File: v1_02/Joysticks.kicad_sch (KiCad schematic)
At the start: 29 parts, among them J10 DB9_Male_MountingHoles, J11 DA15_Socket_MountingHoles, J13 Aliexpress ADS1115 module, J15 Conn_01x01_Pin, J17 Conn_01x03_Pin, U4 74LV165A, U5 74LV165A, U6 LM4040D20ILPR, U7 PCF8583T, Y1 32.768 kHz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

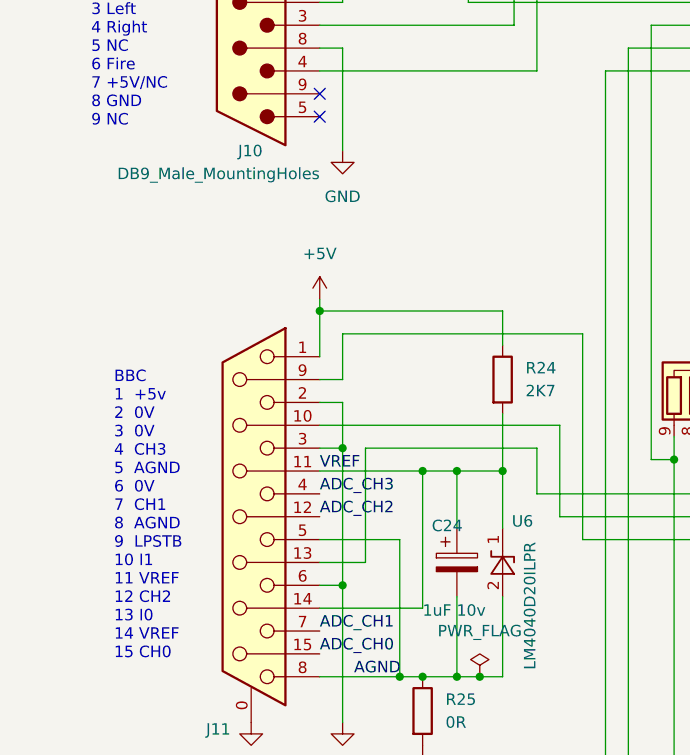
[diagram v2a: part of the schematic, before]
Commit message: v1_02: Increase PS/2 + Tang hole sizes; corrected U6 symbol
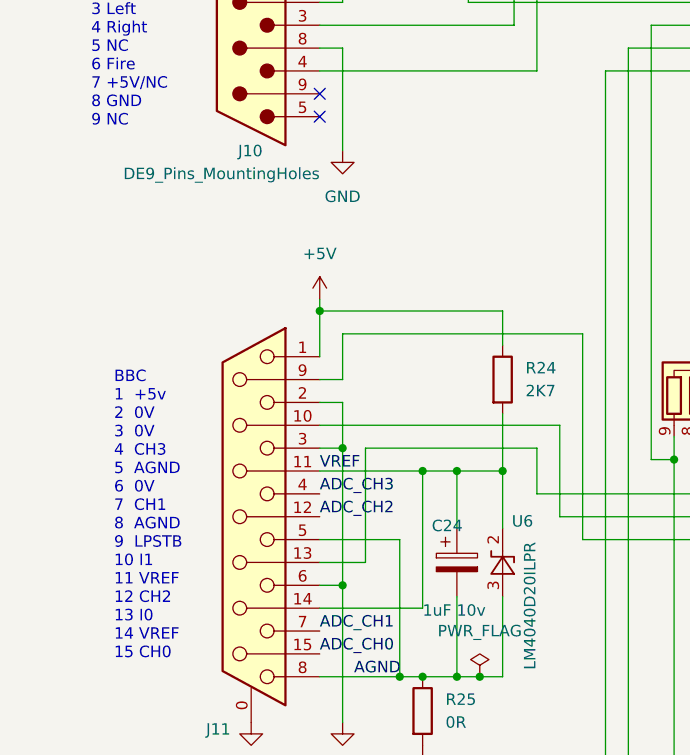
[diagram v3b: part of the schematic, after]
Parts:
- J10: value DB9_Male_MountingHoles -> DE9_Pins_MountingHoles
- U6: footprint Package_TO_SOT_THT:TO-92L_HandSolder -> Package_TO_SOT_THT:TO-92_HandSolder; symbol Reference_Voltage:LM4040DBZ-2.0 -> Reference_Voltage:LM4040LP-2.0
- Y1: footprint Crystal:Crystal_SMD_3215-2Pin_3.2x1.5mm -> TangNano20k:Crystal_SMD_3215-2Pin_3.2x1.5mm
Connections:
- net AGND: now also U6.3 (A); no longer U6.2 (A)
- net VREF: now also U6.2 (K); no longer U6.1 (K)
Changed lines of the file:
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@@
 			)
 		)
-		(property "Footprint" "Crystal:Crystal_SMD_3215-2Pin_3.2x1.5mm"
+		(property "Footprint" "TangNano20k:Crystal_SMD_3215-2Pin_3.2x1.5mm"
 			(at 248.92 106.68 0)
 			(effects
@@
 	)
 	(symbol
-		(lib_id "Reference_Voltage:LM4040DBZ-2.0")
+		(lib_id "Reference_Voltage:LM4040LP-2.0")
 		(at 88.9 111.76 90)
 		(unit 1)
@@
 			)
 		)
-		(property "Footprint" "Package_TO_SOT_THT:TO-92L_HandSolder"
+		(property "Footprint" "Package_TO_SOT_THT:TO-92_HandSolder"
 			(at 93.98 111.76 0)
 			(effects
@@
 			)
 		)
-		(property "Description" "2.048V Precision Micropower Shunt Voltage Reference, SOT-23"
+		(property "Description" "2.048V Precision Micropower Shunt Voltage Reference, TO-92"
 			(at 88.9 111.76 0)
 			(effects
@@
 		)
 		(pin "3"
-		)
-		(pin "1"
 		)
 		(pin "2"
@@
 			)
 		)
-		(property "Value" "DB9_Male_MountingHoles"
+		(property "Value" "DE9_Pins_MountingHoles"
 			(at 68.58 68.58 0)
 			(effects
